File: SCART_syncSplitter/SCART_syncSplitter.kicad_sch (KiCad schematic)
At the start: 1 part, among them U1 EL1883

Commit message: Update the schematic
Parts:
- removed U1: EL1883, Package_SO:SOP-8_3.9x4.9mm_P1.27mm, symbol EL1883:EL1883
- added C1: 570pF / OPEN, symbol Device:C_Small
- added C2, C3, C4: 100nF, symbol Device:C_Small
- added C5: 10uF, symbol Device:C_Polarized_Small
- added J1: SCART-F, symbol Connector:SCART-F
- added J2: DE15_Receptacle_HighDensity_MountingHoles, symbol Connector:DE15_Receptacle_HighDensity_MountingHoles
- added R1: 75, symbol Device:R_Small
- added R2: 100 / SHORT, symbol Device:R_Small
- added R3: 10k 1%, symbol Device:R_Small
- added R4, R6, R8: 100, symbol Device:R_Small
- added R5, R7, R9: 10k/OPEN, symbol Device:R_Small
- added TP1: ODD/EVEN, symbol Connector:TestPoint_Small
- added TP2: BURST, symbol Connector:TestPoint_Small
- added TP3: Video Fmt, symbol Connector:TestPoint_Small
- added U1: ~, Package_SO:TSSOP-14_4.4x5mm_P0.65mm, symbol LMH1981:LMH1981
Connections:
- new net: TP1.1, U1.14 (OE)
- new net: R3.2, U1.1 (Rext)
- new net: C1.1, C2.1, R2.2
- new net: R8.1, U1.7 (HSync)
- new net: R4.1, U1.12 (CSync)
- new net: TP2.1, U1.13 (BP)
- new net: R6.1, U1.8 (VSync)
- new net: TP3.1, U1.9 (VF)
- new net COMPOSITE_IN: R1.1, R2.1
- new net CSync_OUT: R4.2, R5.2
- new net FILT_COMPOSITE: C2.2, U1.4 (Vin)
- new net GND: C1.2, C3.2, C4.1, C5.2, R1.2, R3.1, R5.1, R7.1, R9.1, U1.10 (GND), U1.2 (GND), U1.5 (GND)
- new net HSync_OUT: R8.2, R9.2
- new net VCC: C3.1, C4.2, C5.1, U1.11 (Vcc3), U1.3 (Vcc1), U1.6 (Vcc2)
- new net VSync_OUT: R6.2, R7.2

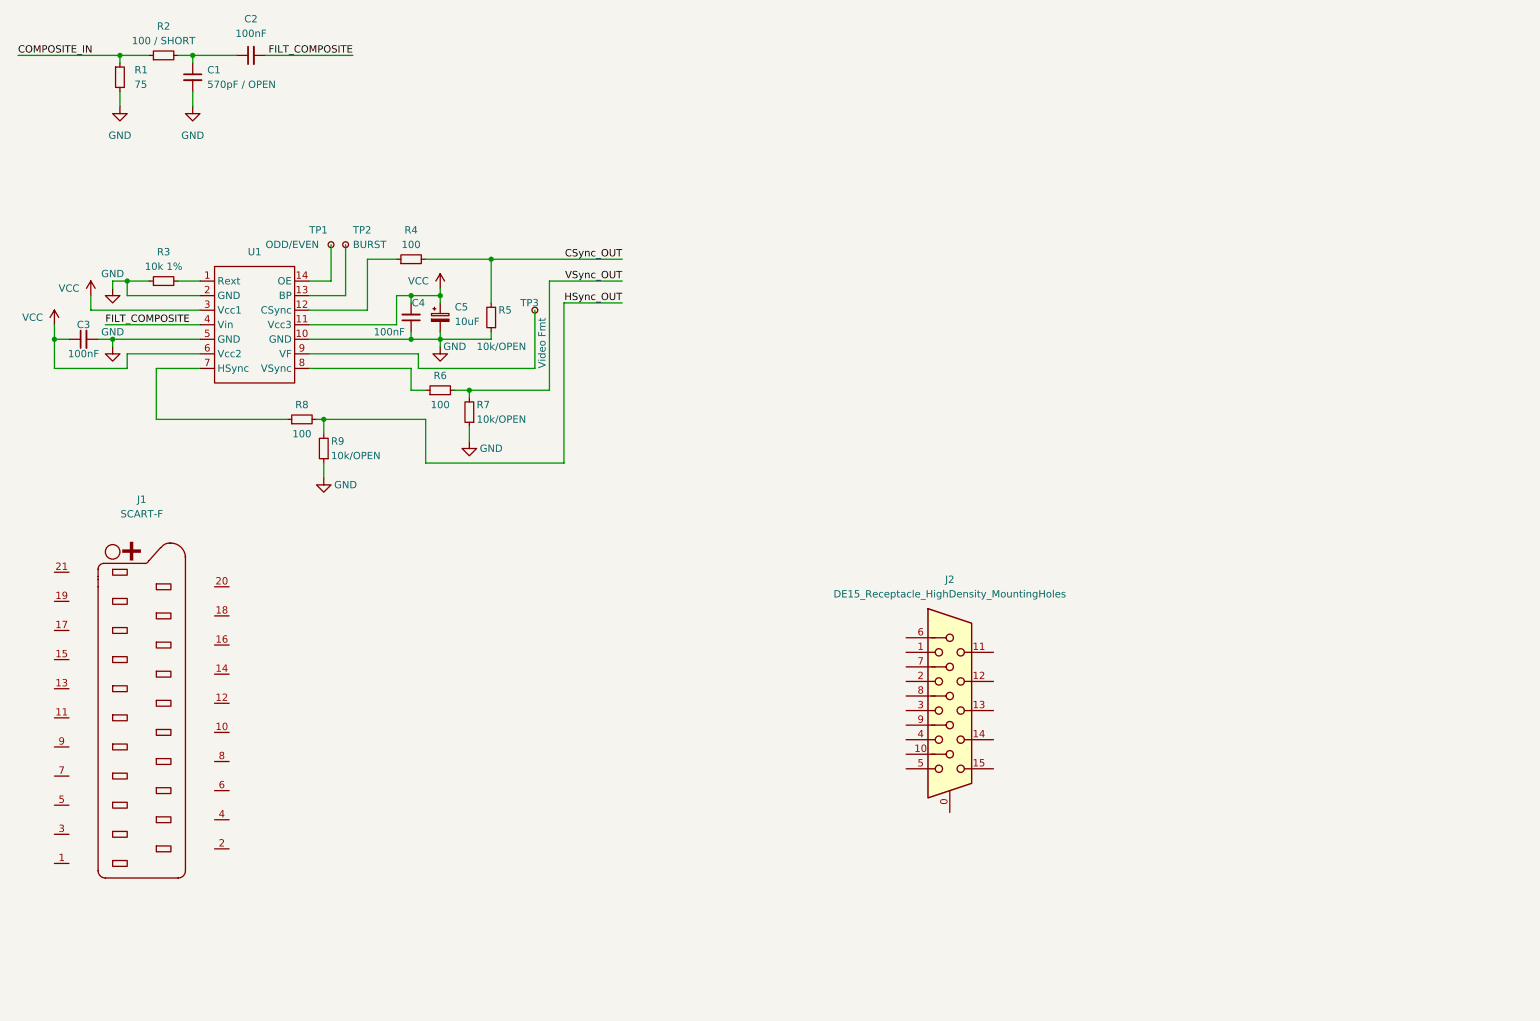
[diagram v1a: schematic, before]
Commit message: Add VGA Out
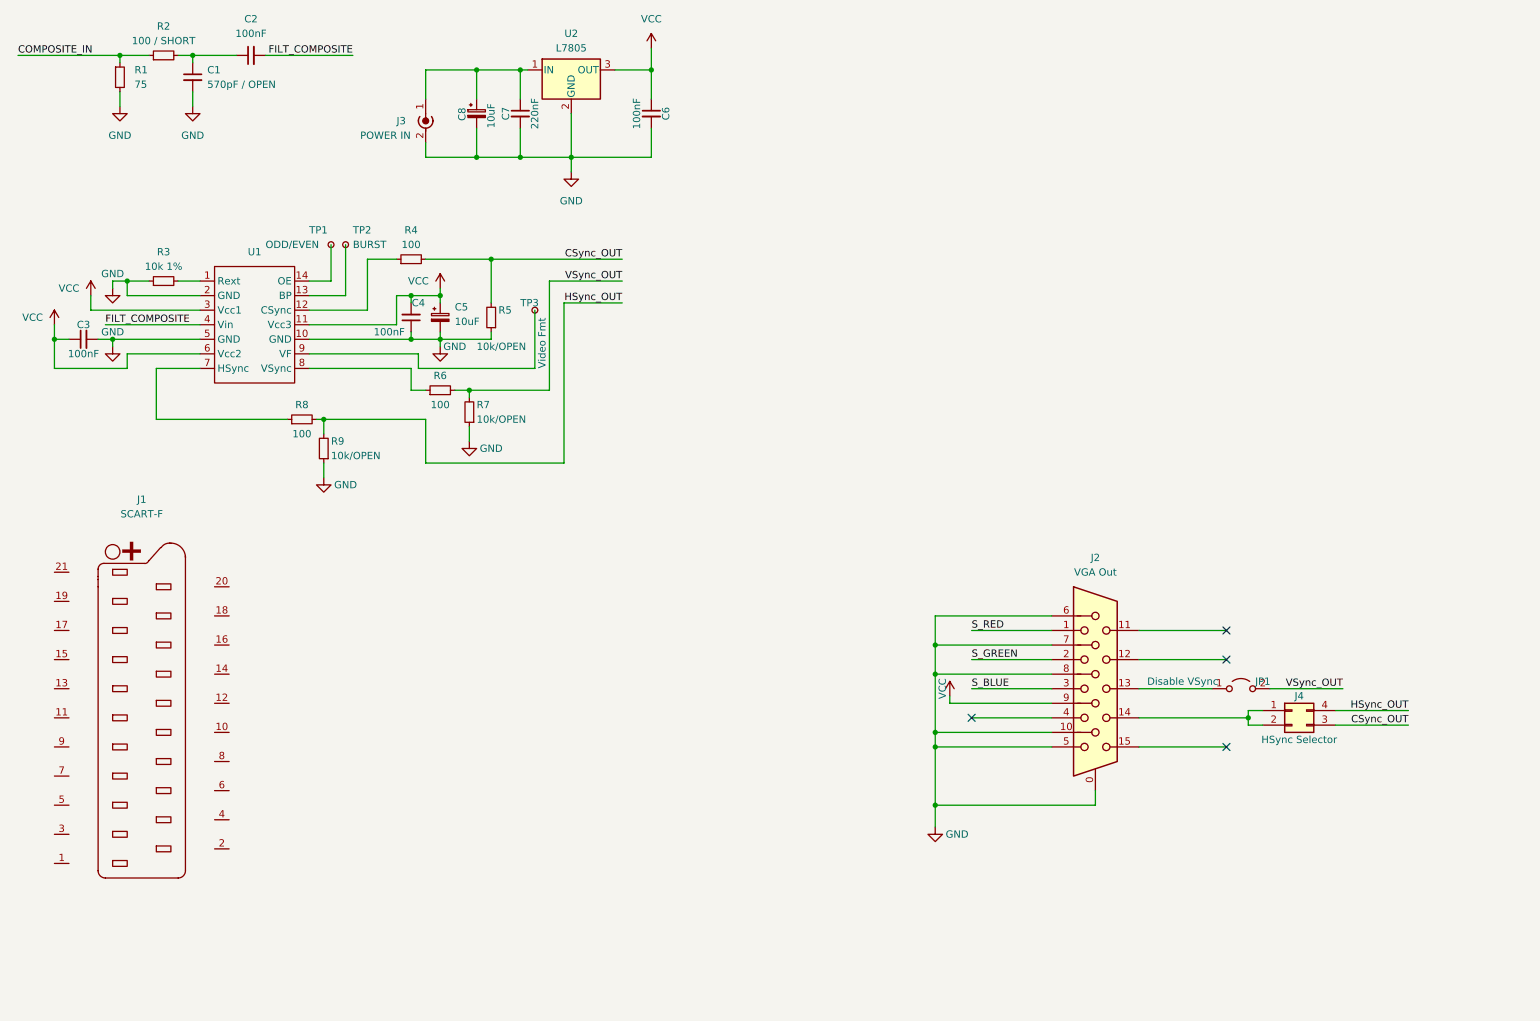
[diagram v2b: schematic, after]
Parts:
- added C6: 100nF, symbol Device:C_Small
- added C7: 220nF, symbol Device:C_Small
- added C8: 10uF, symbol Device:C_Polarized_Small
- added J3: POWER IN, symbol Connector:Conn_Coaxial_Power
- added J4: HSync Selector, symbol Connector_Generic:Conn_02x02_Counter_Clockwise
- added JP1: Disable VSync, symbol Jumper:Jumper_2_Open
- added U2: L7805, symbol Regulator_Linear:L7805
- J2: value DE15_Receptacle_HighDensity_MountingHoles -> VGA Out
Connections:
- net CSync_OUT: now also J4.3 (Pin_3)
- net GND: now also J2.0, J2.10, J2.5, J2.6, J2.7, J2.8, C6.2, C7.2, C8.2, J3.2 (Ext), U2.2 (GND)
- net HSync_OUT: now also J4.4 (Pin_4)
- net VCC: now also J2.9, C6.1, U2.3 (OUT)
- net VSync_OUT: now also JP1.2 (B)
- net S_RED: now reaches J2.1
- net at J2.13: now also JP1.1 (A)
- net at J2.14: now also J4.1 (Pin_1), J4.2 (Pin_2)
- net S_GREEN: now reaches J2.2
- net S_BLUE: now reaches J2.3
- new net: C7.1, C8.1, J3.1 (In), U2.1 (IN)
- no-connect marks 0 -> 4
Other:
- moved on the sheet: J2

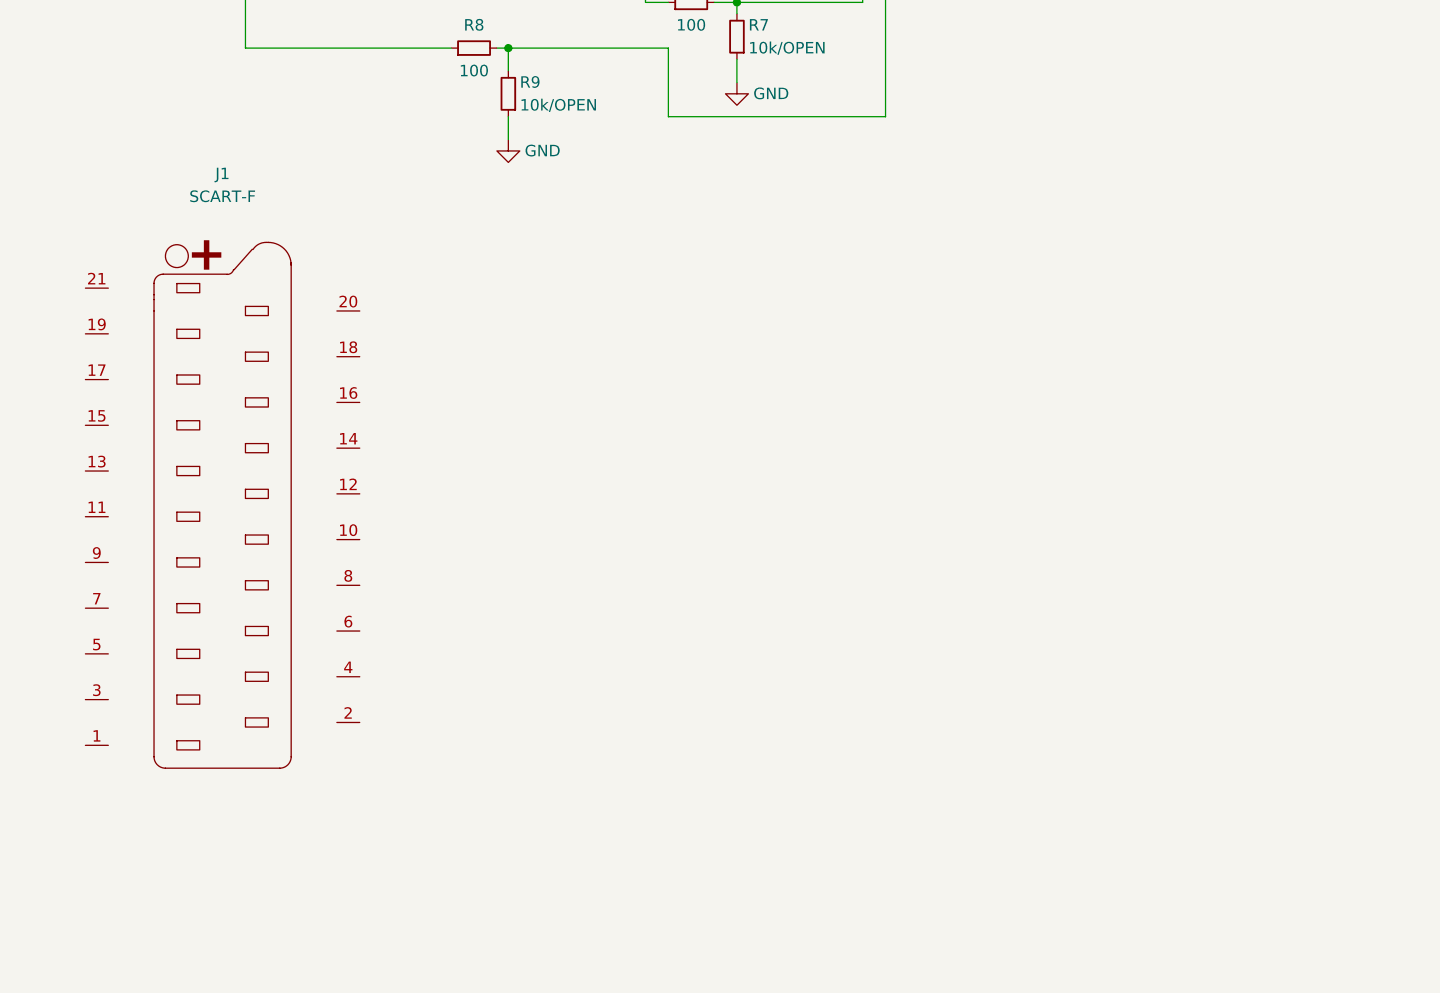
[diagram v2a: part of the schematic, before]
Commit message: Added audio out
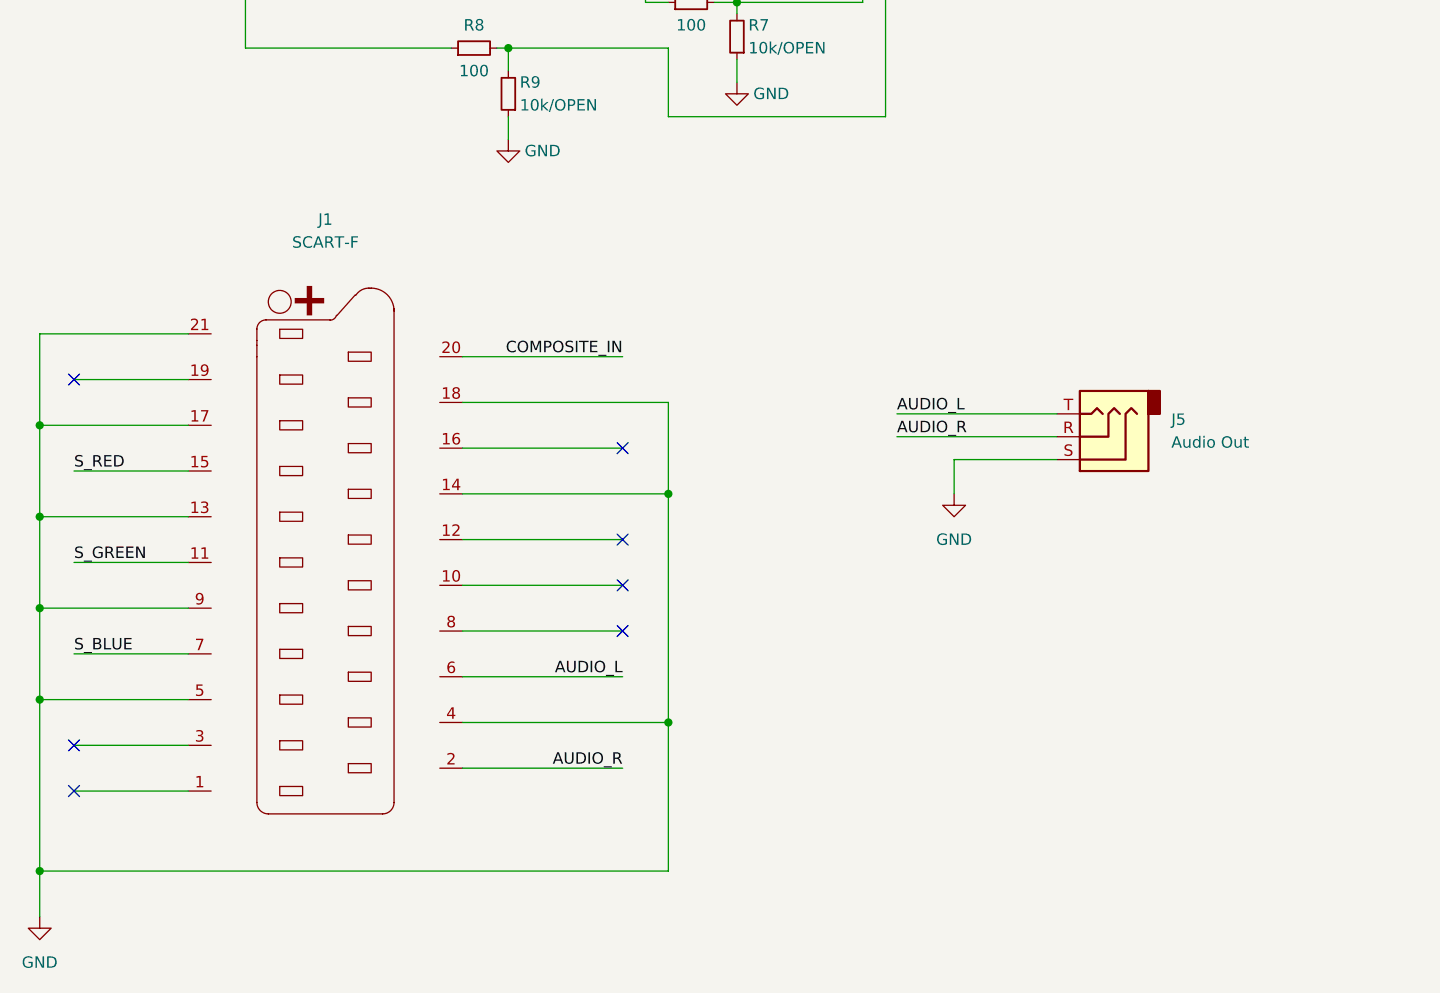
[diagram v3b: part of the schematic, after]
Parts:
- added J5: Audio Out, symbol Connector_Audio:AudioJack3
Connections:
- net COMPOSITE_IN: now also J1.20 (P20)
- net GND: now also J1.13 (P13), J1.14 (P14), J1.17 (P17), J1.18 (P18), J1.21 (P21), J1.4 (P4), J1.5 (P5), J1.9 (P9), J5.S
- net S_BLUE: now also J1.7 (P7)
- net S_GREEN: now also J1.11 (P11)
- net S_RED: now also J1.15 (P15)
- net AUDIO_R: now reaches J1.2 (P2)
- net AUDIO_R: now also J5.R
- net AUDIO_L: now reaches J1.6 (P6)
- net AUDIO_L: now also J5.T
- no-connect marks 4 -> 11
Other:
- moved on the sheet: J1

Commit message: Imported some libraries, started assigning footprints
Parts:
- C1, C2, C3, C4, C6, C7: footprint (none) -> Capacitor_SMD:C_1206_3216Metric_Pad1.33x1.80mm_HandSolder
- J1: footprint (none) -> extron-input:SCART_F_RA
- J5: footprint (none) -> audio:Custom_3.5mm_jack
- R1, R2, R3, R4, R5, R6, R7, R8, R9: footprint (none) -> Resistor_SMD:R_1206_3216Metric_Pad1.30x1.75mm_HandSolder
- U1: value ~ -> LMH1981
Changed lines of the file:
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@@
       (effects (font (size 1.27 1.27)))
     )
-    (property "Footprint" "" (at 29.21 71.12 0)
+    (property "Footprint" "Capacitor_SMD:C_1206_3216Metric_Pad1.33x1.80mm_HandSolder" (at 29.21 71.12 0)
       (effects (font (size 1.27 1.27)) hide)
     )
@@
       (effects (font (size 1.27 1.27)))
     )
-    (property "Footprint" "" (at 43.18 60.96 0)
+    (property "Footprint" "Resistor_SMD:R_1206_3216Metric_Pad1.30x1.75mm_HandSolder" (at 43.18 60.96 0)
       (effects (font (size 1.27 1.27)) hide)
     )
@@
       (effects (font (size 1.27 1.27)))
     )
-    (property "Footprint" "" (at 58.42 21.59 0)
+    (property "Footprint" "Capacitor_SMD:C_1206_3216Metric_Pad1.33x1.80mm_HandSolder" (at 58.42 21.59 0)
       (effects (font (size 1.27 1.27)) hide)
     )
@@
       (effects (font (size 1.27 1.27)))
     )
-    (property "Footprint" "" (at 67.31 85.09 0)
+    (property "Footprint" "Resistor_SMD:R_1206_3216Metric_Pad1.30x1.75mm_HandSolder" (at 67.31 85.09 0)
       (effects (font (size 1.27 1.27)) hide)
     )
@@
       (effects (font (size 1.27 1.27)) (justify right))
     )
-    (property "Footprint" "" (at 137.16 128.27 0)
+    (property "Footprint" "audio:Custom_3.5mm_jack" (at 137.16 128.27 0)
       (effects (font (size 1.27 1.27)) hide)
     )
@@
       (effects (font (size 1.27 1.27)) (justify right))
     )
-    (property "Footprint" "" (at 71.12 90.17 0)
+    (property "Footprint" "Resistor_SMD:R_1206_3216Metric_Pad1.30x1.75mm_HandSolder" (at 71.12 90.17 0)
       (effects (font (size 1.27 1.27)) hide)
     )
@@
       (effects (font (size 1.27 1.27)))
     )
-    (property "Footprint" "" (at 86.36 57.15 0)
+    (property "Footprint" "Resistor_SMD:R_1206_3216Metric_Pad1.30x1.75mm_HandSolder" (at 86.36 57.15 0)
       (effects (font (size 1.27 1.27)) hide)
     )
@@
   )
   (symbol (lib_id "LMH1981:LMH1981") (at 59.69 68.58 0) (unit 1)
-    (in_bom yes) (on_board yes) (dnp no) (fields_autoplaced)
-    (property "Reference" "U1" (at 59.055 55.88 0)
-      (effects (font (size 1.27 1.27)))
-    )
-    (property "Value" "~" (at 68.58 57.15 0)
+    (in_bom yes) (on_board yes) (dnp no)
+    (property "Reference" "U1" (at 54.61 57.15 0)
+      (effects (font (size 1.27 1.27)))
+    )
+    (property "Value" "LMH1981" (at 58.42 80.01 0)
       (effects (font (size 1.27 1.27)))
     )
@@
       (effects (font (size 1.27 1.27)) (justify left))
     )
-    (property "Footprint" "" (at 35.56 25.4 0)
+    (property "Footprint" "Resistor_SMD:R_1206_3216Metric_Pad1.30x1.75mm_HandSolder" (at 35.56 25.4 0)
       (effects (font (size 1.27 1.27)) hide)
     )
@@
       (effects (font (size 1.27 1.27)) (justify right))
     )
-    (property "Footprint" "" (at 100.33 67.31 0)
+    (property "Footprint" "Resistor_SMD:R_1206_3216Metric_Pad1.30x1.75mm_HandSolder" (at 100.33 67.31 0)
       (effects (font (size 1.27 1.27)) hide)
     )
@@
       (effects (font (size 1.27 1.27)))
     )
-    (property "Footprint" "" (at 43.18 21.59 0)
+    (property "Footprint" "Resistor_SMD:R_1206_3216Metric_Pad1.30x1.75mm_HandSolder" (at 43.18 21.59 0)
       (effects (font (size 1.27 1.27)) hide)
     )
@@
       (effects (font (size 1.27 1.27)))
     )
-    (property "Footprint" "" (at 86.36 67.31 0)
+    (property "Footprint" "Capacitor_SMD:C_1206_3216Metric_Pad1.33x1.80mm_HandSolder" (at 86.36 67.31 0)
       (effects (font (size 1.27 1.27)) hide)
     )
@@
       (effects (font (size 1.27 1.27)) (justify left))
     )
-    (property "Footprint" "" (at 48.26 25.4 0)
+    (property "Footprint" "Capacitor_SMD:C_1206_3216Metric_Pad1.33x1.80mm_HandSolder" (at 48.26 25.4 0)
       (effects (font (size 1.27 1.27)) hide)
     )
@@
       (effects (font (size 1.27 1.27)))
     )
-    (property "Footprint" "" (at 105.41 31.75 0)
+    (property "Footprint" "Capacitor_SMD:C_1206_3216Metric_Pad1.33x1.80mm_HandSolder" (at 105.41 31.75 0)
       (effects (font (size 1.27 1.27)) hide)
     )
@@
       (effects (font (size 1.27 1.27)))
     )
-    (property "Footprint" "" (at 128.27 31.75 0)
+    (property "Footprint" "Capacitor_SMD:C_1206_3216Metric_Pad1.33x1.80mm_HandSolder" (at 128.27 31.75 0)
       (effects (font (size 1.27 1.27)) hide)
     )
@@
       (effects (font (size 1.27 1.27)))
     )
-    (property "Footprint" "" (at 50.8 140.97 0)
+    (property "Footprint" "extron-input:SCART_F_RA" (at 50.8 140.97 0)
       (effects (font (size 1.27 1.27)) hide)
     )
@@
       (effects (font (size 1.27 1.27)))
     )
-    (property "Footprint" "" (at 91.44 80.01 0)
+    (property "Footprint" "Resistor_SMD:R_1206_3216Metric_Pad1.30x1.75mm_HandSolder" (at 91.44 80.01 0)
       (effects (font (size 1.27 1.27)) hide)
     )
@@
       (effects (font (size 1.27 1.27)) (justify right))
     )
-    (property "Footprint" "" (at 96.52 83.82 0)
-      (effects (font (size 1.27 1.27)) hide)
-    )
+    (property "Footprint" "Resistor_SMD:R_1206_3216Metric_Pad1.30x1.75mm_HandSolder" (at 96.52 83.82 0)
+      (effects (font (size 1.27 1.27)) hide)
+    )
